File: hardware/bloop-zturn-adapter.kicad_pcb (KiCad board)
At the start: 2 copper layers, 3 parts, among them J2 Z-Turn CN2, P2 BLOOP SPI CONTROL, P3 BLOOP SPI CONTROL

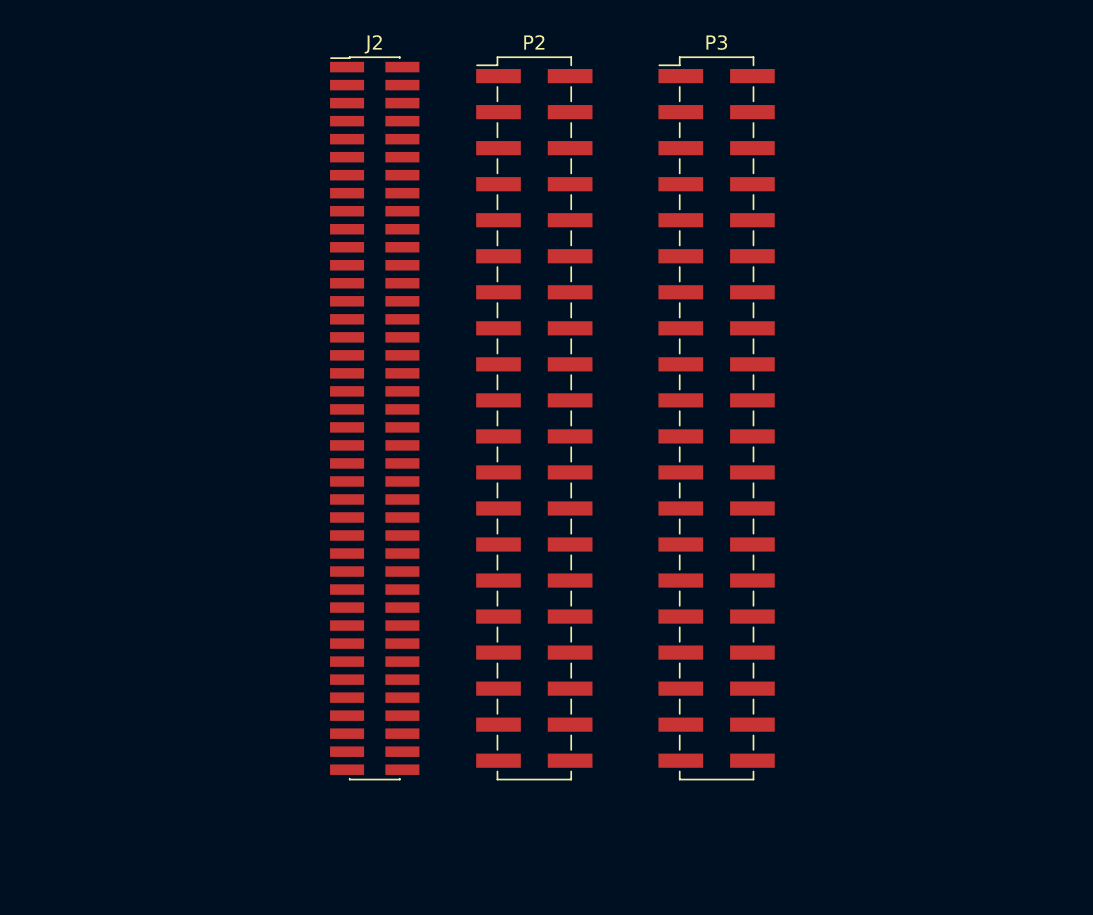
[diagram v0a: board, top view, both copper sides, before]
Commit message: Schematic edits to make layout routing easier and completed layout. Generated gerbers and pdf schematic.
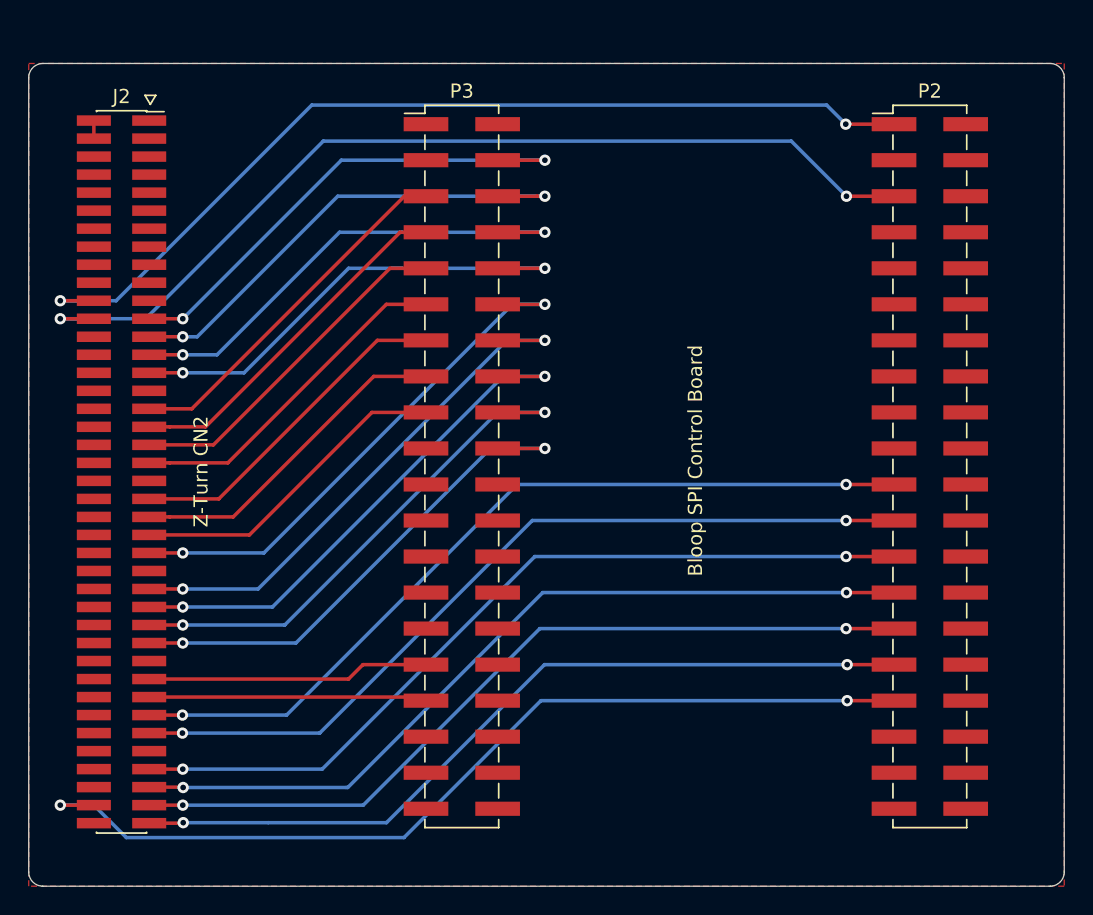
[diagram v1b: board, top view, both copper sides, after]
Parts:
- moved P2 28.1 mm to (172.4, 93.1)
- moved P3 18.3 mm to (139.4, 93.1)
- moved J2 18.2 mm to (115.4, 93.5)
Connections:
- J2 pad 22: /~RESET\PWDN -> /DATA_READY
- J2 pad 23: /ADC_DOUT7 -> /ADC_DOUT0
- J2 pad 24: /~FAULT -> /MCLKIN
- J2 pad 25: /ADC_DOUT6 -> /ADC_DOUT1
- J2 pad 26: /PLL_LE -> /IO_B35_LP4
- J2 pad 27: /ADC_DOUT5 -> /ADC_DOUT2
- J2 pad 29: /ADC_DOUT4 -> /ADC_DOUT3
- J2 pad 33: /ADC_DOUT3 -> /ADC_DOUT4
- J2 pad 35: /ADC_DOUT2 -> /ADC_DOUT5
- J2 pad 37: /ADC_DOUT1 -> /ADC_DOUT6
- J2 pad 39: /ADC_DOUT0 -> /ADC_DOUT7
- J2 pad 43: /SCLK_ADC -> /PLL_LE
- J2 pad 45: /MCLKIN -> /PLL_DIV_MCU
- J2 pad 47: /DATA_READY -> /PLL_CS
- J2 pad 49: /~CONV_START -> /SCLK_ADC
- J2 pad 51: +3V3 -> Net-(J2-Pad51)
- J2 pad 53: /SCK -> /~CONV_START
- J2 pad 55: /MISO -> /SCK
- J2 pad 57: /MOSI -> /MISO
- J2 pad 59: /PLL_CS -> /MOSI
- J2 pad 63: /~ADC_CS -> /~FAULT
- J2 pad 65: /~BGT_CS -> /~RESET\PWDN
- J2 pad 67: /PLL_DIV_MCU -> /PLL_MOD
- J2 pad 69: /PLL_MOD -> /PLL_MUX
- J2 pad 73: /PLL_MUX -> /PLL_RSET
- J2 pad 78: /IO_B35_LN24 -> /~BGT_CS
- J2 pad 79: /PLL_RSET -> /~ADC_CS
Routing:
- net /MCLKIN: track 0.00 -> 67.9 mm, vias 0 -> 2
- net /DATA_READY: track 0.00 -> 67.4 mm, vias 0 -> 2
- net /~BGT_CS: track 0.00 -> 66.1 mm, vias 0 -> 2
- net /PLL_MOD: track 0.00 -> 59.2 mm, vias 0 -> 2
- net /PLL_MUX: track 0.00 -> 58.7 mm, vias 0 -> 2
- net /PLL_RSET: track 0.00 -> 58.7 mm, vias 0 -> 2
- net /PLL_TRIG2: track 0.00 -> 58.2 mm, vias 0 -> 2
- net /PLL_TRIG1: track 0.00 -> 57.7 mm, vias 0 -> 2
- net /~ADC_CS: track 0.00 -> 57.1 mm, vias 0 -> 2
- net /~CONV_START: track 0.00 -> 38.5 mm, vias 0 -> 2
- net /SCLK_ADC: track 0.00 -> 38.5 mm, vias 0 -> 2
- net /SCK: track 0.00 -> 38.0 mm, vias 0 -> 2
- net /MISO: track 0.00 -> 37.4 mm, vias 0 -> 2
- net /MOSI: track 0.00 -> 36.9 mm, vias 0 -> 2
- net /ADC_DOUT0: track 0.00 -> 35.9 mm, vias 0 -> 2
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- added copper zone on F.Cu, net GND
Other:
- board outline added: 73 x 58 mm
- board text added: "Bloop SPI Control Board"
- board text added: "Bloop Z-Turn Adapter Rev A"
- board text added: "Z-Turn CN2"
